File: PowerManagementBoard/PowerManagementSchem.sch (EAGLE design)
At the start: 122 parts, among them J1 D15S24A4GV00LF, J8 182-037-213R531, J9 182-025-213R531, Q1 PMOSFET, Q10 PMOSFET, Q11 PMOSFET, Q12 PMOSFET, Q2 PMOSFET, Q3 PMOSFET, Q4 PMOSFET, Q5 PMOSFET, Q6 PMOSFET, Q7 PMOSFET, Q8 PMOSFET, Q9 PMOSFET, U1 VX7805-500, U2 PYB20-Q24-S5, U3 PYB30-Q48-S5, U4 PYB30-Q48-S12, U5 3V3REG, U6 INA4180-SPLIT, U7 INA4180-SPLIT, U8 TEENSY-4.0SILK, U9 INA4180-SPLIT

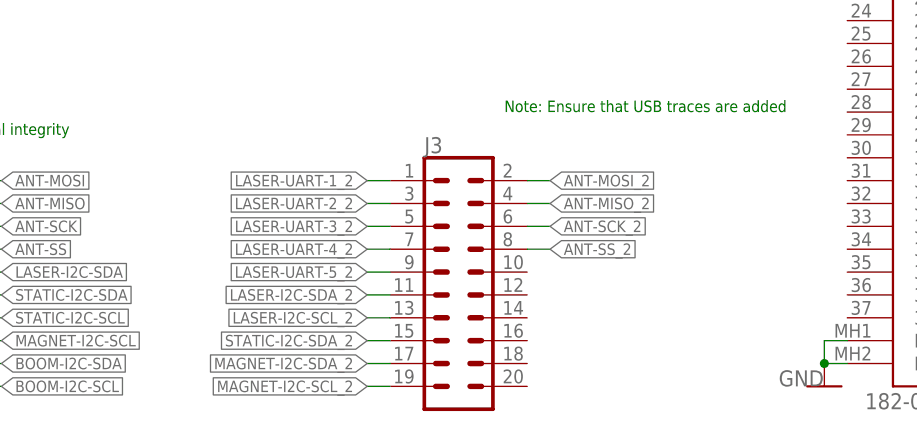
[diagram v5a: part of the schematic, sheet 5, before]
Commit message: Some traces routed on Pwr Distrib. board
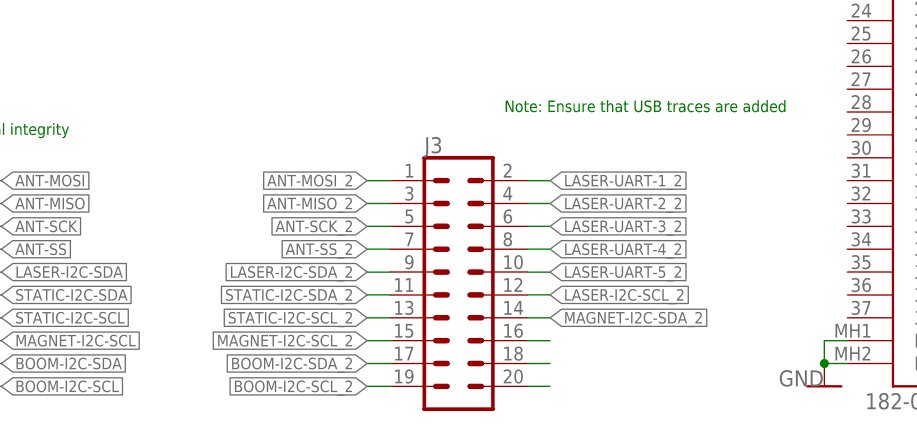
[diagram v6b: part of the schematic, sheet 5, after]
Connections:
- new net BOOM-I2C-SCL_2: J3.19
- new net BOOM-I2C-SDA_2: J3.17
- new net N$33: J3.18
- new net N$37: J3.20
- new net N$7: J3.16
- new net STATIC-I2C-SCL_2: J3.13
- net ANT-MISO_2: now also J3.3; no longer J3.4
- net ANT-MOSI_2: now also J3.1; no longer J3.2
- net ANT-SCK_2: now also J3.5; no longer J3.6
- net ANT-SS_2: now also J3.7; no longer J3.8
- net LASER-I2C-SCL_2: now also J3.12; no longer J3.13
- net LASER-I2C-SDA_2: now also J3.9; no longer J3.11
- net LASER-UART-1_2: now also J3.2; no longer J3.1
- net LASER-UART-2_2: now also J3.4; no longer J3.3
- net LASER-UART-3_2: now also J3.6; no longer J3.5
- net LASER-UART-4_2: now also J3.8; no longer J3.7
- net LASER-UART-5_2: now also J3.10; no longer J3.9
- net MAGNET-I2C-SCL_2: now also J3.15; no longer J3.19
- net MAGNET-I2C-SDA_2: now also J3.14; no longer J3.17
- net STATIC-I2C-SDA_2: now also J3.11; no longer J3.15
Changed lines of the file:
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@@
 <?xml version="1.0" encoding="utf-8"?>
 <!DOCTYPE eagle SYSTEM "eagle.dtd">
-<eagle version="9.4.2">
+<eagle version="9.5.2">
 <drawing>
 <settings>
@@
 <net name="LASER-UART-1_2" class="0">
 <segment>
+<pinref part="J3" gate="G$1" pin="2"/>
+<wire x1="111.76" y1="33.02" x2="114.3" y2="33.02" width="0.1524" layer="91"/>
+<label x="114.3" y="33.02" size="1.27" layer="95" xref="yes"/>
+</segment>
+</net>
+<net name="LASER-UART-2_2" class="0">
+<segment>
+<pinref part="J3" gate="G$1" pin="4"/>
+<wire x1="111.76" y1="30.48" x2="114.3" y2="30.48" width="0.1524" layer="91"/>
+<label x="114.3" y="30.48" size="1.27" layer="95" xref="yes"/>
+</segment>
+</net>
+<net name="LASER-UART-3_2" class="0">
+<segment>
+<pinref part="J3" gate="G$1" pin="6"/>
+<wire x1="111.76" y1="27.94" x2="114.3" y2="27.94" width="0.1524" layer="91"/>
+<label x="114.3" y="27.94" size="1.27" layer="95" xref="yes"/>
+</segment>
+</net>
+<net name="LASER-UART-4_2" class="0">
+<segment>
+<pinref part="J3" gate="G$1" pin="8"/>
+<wire x1="111.76" y1="25.4" x2="114.3" y2="25.4" width="0.1524" layer="91"/>
+<label x="114.3" y="25.4" size="1.27" layer="95" xref="yes"/>
+</segment>
+</net>
+<net name="LASER-UART-5_2" class="0">
+<segment>
+<pinref part="J3" gate="G$1" pin="10"/>
+<wire x1="111.76" y1="22.86" x2="114.3" y2="22.86" width="0.1524" layer="91"/>
+<label x="114.3" y="22.86" size="1.27" layer="95" xref="yes"/>
+</segment>
+</net>
+<net name="LASER-I2C-SCL_2" class="0">
+<segment>
+<pinref part="J3" gate="G$1" pin="12"/>
+<wire x1="111.76" y1="20.32" x2="114.3" y2="20.32" width="0.1524" layer="91"/>
+<label x="114.3" y="20.32" size="1.27" layer="95" xref="yes"/>
+</segment>
+</net>
+<net name="MAGNET-I2C-SDA_2" class="0">
+<segment>
+<pinref part="J3" gate="G$1" pin="14"/>
+<wire x1="111.76" y1="17.78" x2="114.3" y2="17.78" width="0.1524" layer="91"/>
+<label x="114.3" y="17.78" size="1.27" layer="95" xref="yes"/>
+</segment>
+</net>
+<net name="N$7" class="0">
+<segment>
+<pinref part="J3" gate="G$1" pin="16"/>
+<wire x1="111.76" y1="15.24" x2="114.3" y2="15.24" width="0.1524" layer="91"/>
+</segment>
+</net>
+<net name="N$33" class="0">
+<segment>
+<pinref part="J3" gate="G$1" pin="18"/>
+<wire x1="111.76" y1="12.7" x2="114.3" y2="12.7" width="0.1524" layer="91"/>
+</segment>
+</net>
+<net name="N$37" class="0">
+<segment>
+<pinref part="J3" gate="G$1" pin="20"/>
+<wire x1="111.76" y1="10.16" x2="114.3" y2="10.16" width="0.1524" layer="91"/>
+</segment>
+</net>
+<net name="ANT-MOSI_2" class="0">
+<segment>
 <pinref part="J3" gate="G$1" pin="1"/>
 <wire x1="96.52" y1="33.02" x2="93.98" y2="33.02" width="0.1524" layer="91"/>
@@
 </segment>
 </net>
-<net name="LASER-UART-2_2" class="0">
+<net name="ANT-MISO_2" class="0">
 <segment>
 <pinref part="J3" gate="G$1" pin="3"/>
@@
 </segment>
 </net>
-<net name="LASER-UART-3_2" class="0">
+<net name="ANT-SCK_2" class="0">
 <segment>
 <pinref part="J3" gate="G$1" pin="5"/>
@@
 </segment>
 </net>
-<net name="LASER-UART-4_2" class="0">
+<net name="ANT-SS_2" class="0">
 <segment>
 <pinref part="J3" gate="G$1" pin="7"/>
@@
 </segment>
 </net>
-<net name="LASER-UART-5_2" class="0">
+<net name="LASER-I2C-SDA_2" class="0">
 <segment>
 <pinref part="J3" gate="G$1" pin="9"/>
@@
 </segment>
 </net>
-<net name="LASER-I2C-SDA_2" class="0">
+<net name="STATIC-I2C-SDA_2" class="0">
 <segment>
 <pinref part="J3" gate="G$1" pin="11"/>
@@
 </segment>
 </net>
-<net name="LASER-I2C-SCL_2" class="0">
+<net name="STATIC-I2C-SCL_2" class="0">
 <segment>
 <pinref part="J3" gate="G$1" pin="13"/>
@@
 </segment>
 </net>
-<net name="STATIC-I2C-SDA_2" class="0">
+<net name="MAGNET-I2C-SCL_2" class="0">
 <segment>
 <pinref part="J3" gate="G$1" pin="15"/>
@@
 </segment>
 </net>
-<net name="MAGNET-I2C-SDA_2" class="0">
+<net name="BOOM-I2C-SDA_2" class="0">
 <segment>
 <pinref part="J3" gate="G$1" pin="17"/>
@@
 </segment>
 </net>
-<net name="MAGNET-I2C-SCL_2" class="0">
+<net name="BOOM-I2C-SCL_2" class="0">
 <segment>
 <pinref part="J3" gate="G$1" pin="19"/>
@@
 </segment>
 </net>
-<net name="ANT-MOSI_2" class="0">
-<segment>
-<pinref part="J3" gate="G$1" pin="2"/>
-<wire x1="111.76" y1="33.02" x2="114.3" y2="33.02" width="0.1524" layer="91"/>
-<label x="114.3" y="33.02" size="1.27" layer="95" xref="yes"/>
-</segment>
-</net>
-<net name="ANT-MISO_2" class="0">
-<segment>
-<pinref part="J3" gate="G$1" pin="4"/>
-<wire x1="111.76" y1="30.48" x2="114.3" y2="30.48" width="0.1524" layer="91"/>
-<label x="114.3" y="30.48" size="1.27" layer="95" xref="yes"/>
-</segment>
-</net>
-<net name="ANT-SCK_2" class="0">
-<segment>
-<pinref part="J3" gate="G$1" pin="6"/>
-<wire x1="111.76" y1="27.94" x2="114.3" y2="27.94" width="0.1524" layer="91"/>
-<label x="114.3" y="27.94" size="1.27" layer="95" xref="yes"/>
-</segment>
-</net>
-<net name="ANT-SS_2" class="0">
-<segment>
-<pinref part="J3" gate="G$1" pin="8"/>
-<wire x1="111.76" y1="25.4" x2="114.3" y2="25.4" width="0.1524" layer="91"/>
-<label x="114.3" y="25.4" size="1.27" layer="95" xref="yes"/>
-</segment>
-</net>

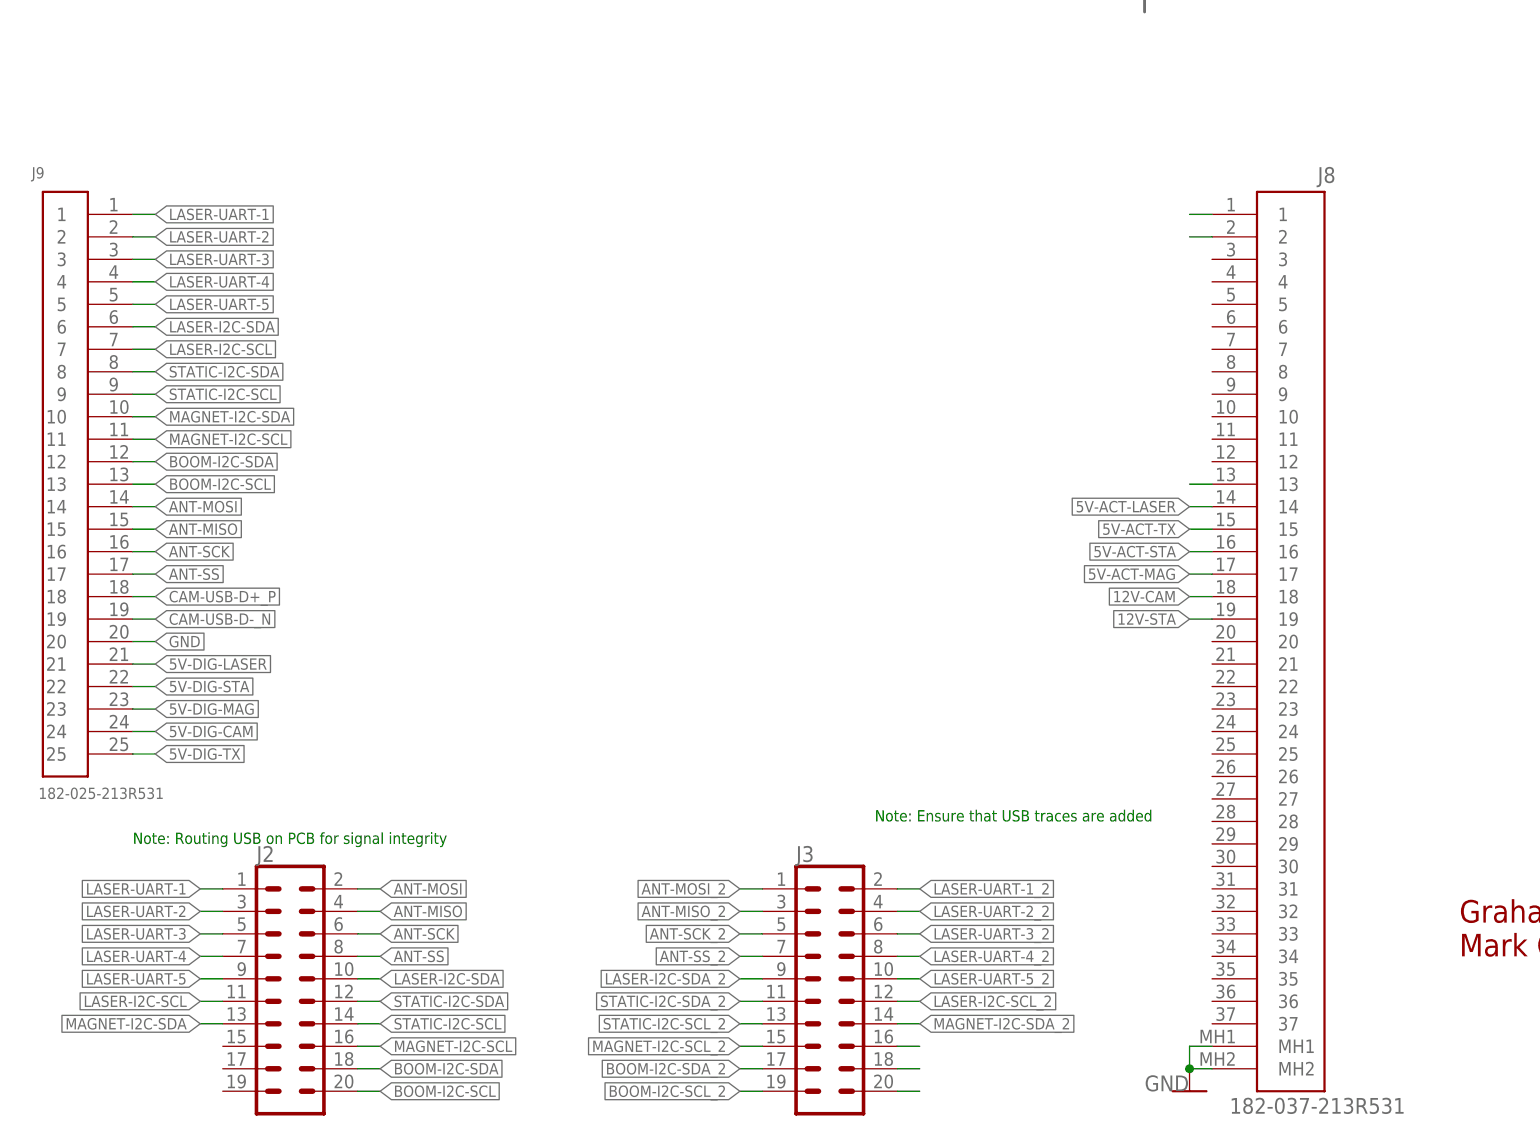
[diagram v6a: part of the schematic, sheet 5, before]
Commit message: Amost all of pwr board routed. Pushing for safety before MOSFET control pin rework.
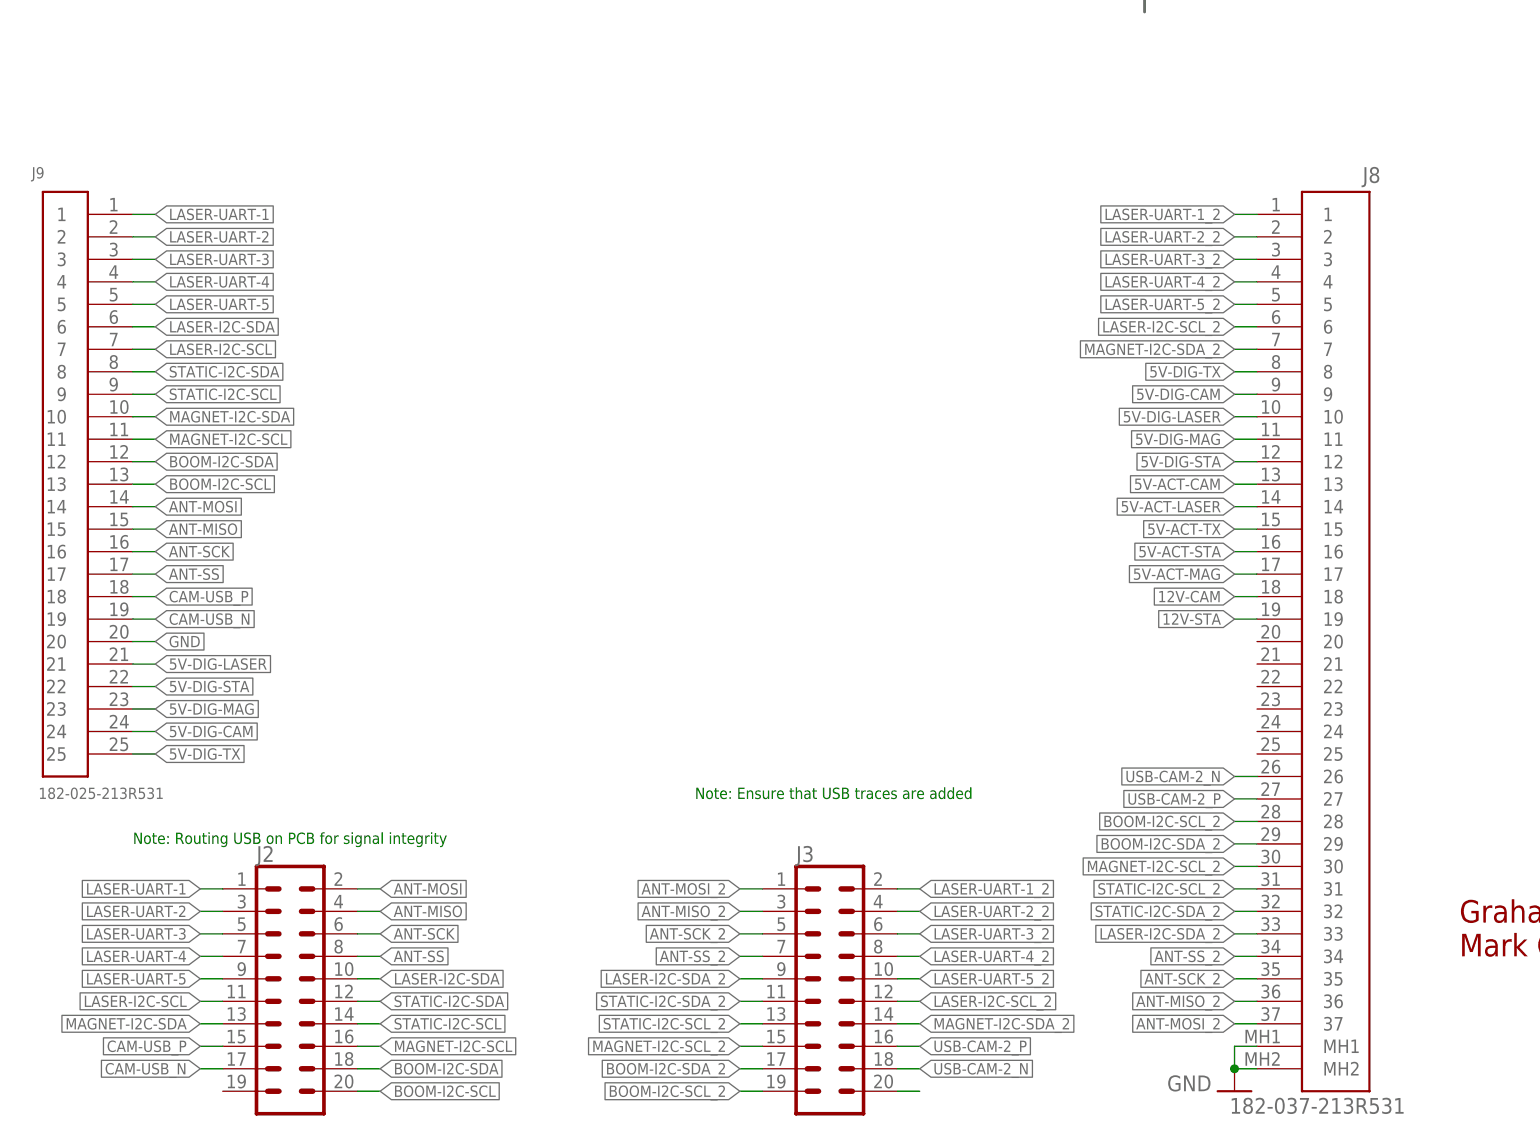
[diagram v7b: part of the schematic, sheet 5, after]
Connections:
- removed net CAM-USB-D+_P: J9.18
- removed net CAM-USB-D-_N: J9.19
- removed net N$1: J8.1
- removed net N$2: J8.2
- removed net N$33: J3.18
- removed net N$35: J8.13
- removed net N$7: J3.16
- new net CAM-USB_N: J2.17, J9.19
- new net CAM-USB_P: J2.15, J9.18
- new net USB-CAM-2_N: J3.18, J8.26
- new net USB-CAM-2_P: J3.16, J8.27
- net 5V-ACT-CAM: now also J8.13
- net 5V-DIG-CAM: now also J8.9
- net 5V-DIG-LASER: now also J8.10
- net 5V-DIG-MAG: now also J8.11
- net 5V-DIG-STA: now also J8.12
- net 5V-DIG-TX: now also J8.8
- net ANT-MISO_2: now also J8.36
- net ANT-MOSI_2: now also J8.37
- net ANT-SCK_2: now also J8.35
- net ANT-SS_2: now also J8.34
- net BOOM-I2C-SCL_2: now also J8.28
- net BOOM-I2C-SDA_2: now also J8.29
- net LASER-I2C-SCL_2: now also J8.6
- net LASER-I2C-SDA_2: now also J8.33
- net LASER-UART-1_2: now also J8.1
- net LASER-UART-2_2: now also J8.2
- net LASER-UART-3_2: now also J8.3
- net LASER-UART-4_2: now also J8.4
- net LASER-UART-5_2: now also J8.5
- net MAGNET-I2C-SCL_2: now also J8.30
- net MAGNET-I2C-SDA_2: now also J8.7
- net STATIC-I2C-SCL_2: now also J8.31
- net STATIC-I2C-SDA_2: now also J8.32
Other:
- moved on the sheet: J8
